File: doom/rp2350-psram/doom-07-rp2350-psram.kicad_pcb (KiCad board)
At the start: 4 copper layers, 144 x 110 mm, 100 parts, among them J4 DM3AT-SF-PEJM5, J5 S2B-PH-K-S(LF)(SN), Q1 AO3401A, Q2 FS8205A, SW1 PTS645SM43SMTR92 LFS, SW10 PTS645SM43SMTR92 LFS, SW11 PTS645SM43SMTR92 LFS, SW12 MSK12C02, SW2 PTS645SM43SMTR92 LFS, SW3 PTS645SM43SMTR92 LFS, SW4 PTS645SM43SMTR92 LFS, SW5 PTS645SM43SMTR92 LFS, SW6 PTS645SM43SMTR92 LFS, SW7 PTS645SM43SMTR92 LFS, SW8 PTS645SM43SMTR92 LFS, SW9 PTS645SM43SMTR92 LFS, U1 RP2350A, U2 W25Q128JVSIQ, U3 APS6404L-3SQR-SN, U4 TLV75533PDBVR, U5 MAX98357AETE+T, U6 BQ24075RGTR, U7 MAX17048G+T10, U8 DW01A, U9 ESD 2-line, Y1 12MHz 10pF

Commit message: doom, examples: re-route around the USB-C receptacle's new land pattern
The standard receptacle became GCT USB4105's recommended layout (pcbkit 7e43c086): its shield
legs moved and two unplated guide holes appeared, under the copper these boards had been routed
with (solder-mask-bridge and clearance errors at J1). `build.run` re-routed the 3–5 nets that
crossed it: all seven check complete with 0 errors again; the six Doom boards export for the fab
without --force.

Claude-Session: https://claude.ai/code/session_01GffCzZXi9ShujPbky1eccg
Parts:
- F1: value PTC 1000mA -> PTC 750mA
- J1: value (none) -> USB4105-GF-A
- U9: value ESD 2-line -> USBLC6-2SC6
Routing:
- net DN: track 52.0 -> 50.7 mm
- net DP: track 64.5 -> 65.3 mm
- net SYS: track 211.8 -> 211.2 mm
- net GND: track 17.2 -> 17.7 mm, vias 20 -> 21

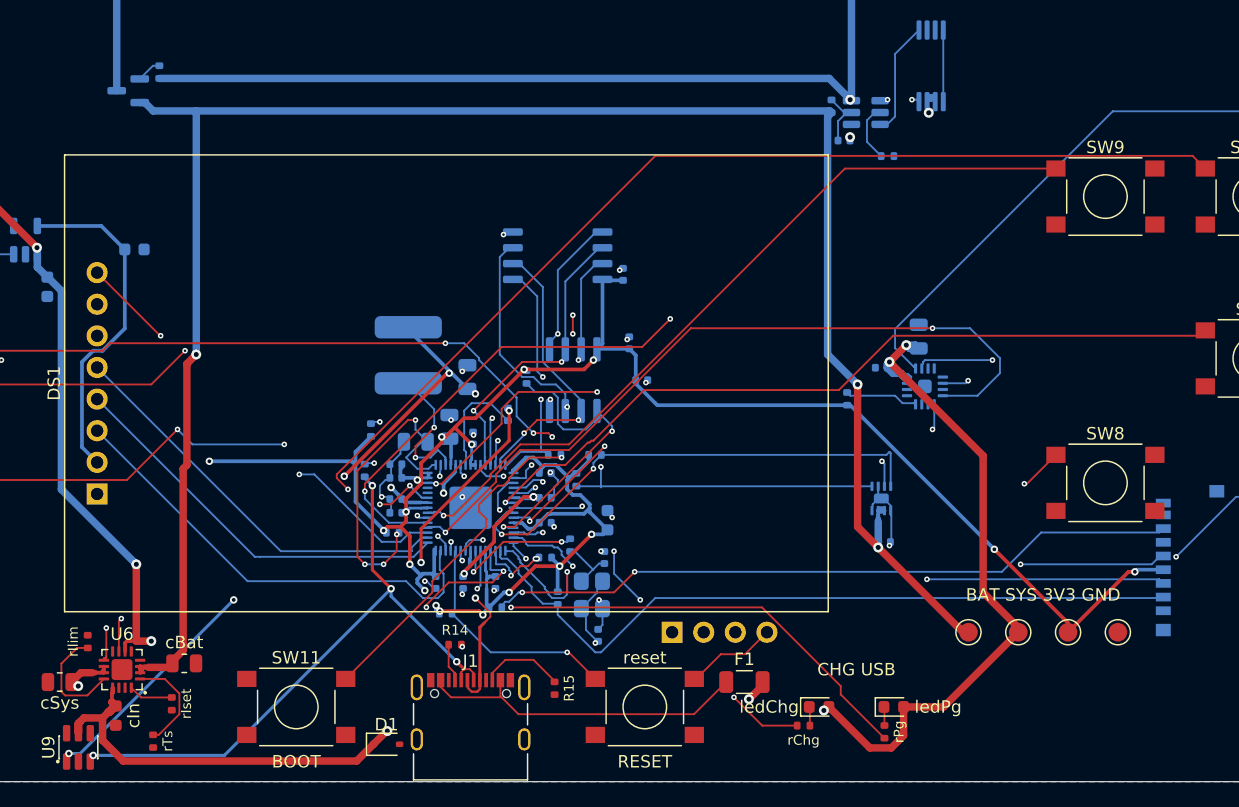
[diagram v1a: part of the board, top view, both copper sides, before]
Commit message: Boards pass check and KiCad 10's DRC again: holes in courtyards, the USB net rename
pcbkit's check now has KiCad 10's pth/npth_inside_courtyard (pcbkit be5b6955), and 13 boards
failed it. KiCad's own DRC (kicad-cli 10) reports the same holes on every one of them.

- Parts that really stand above the holes under them (a screen or a Nano on its sockets, the
  Delta-S02's КМ-6 capacitors flat under its chips, as the factory placed them): a courtyard rule
  for the pair, written to each board's .kicad_dru, so KiCad's DRC agrees.
- Real collisions moved: servo-controller's dial 3 mm up (the Nano's socket pins came out under
  it), c3-pocket's fourth M3 hole from under a cell holder to the top edge's middle, s3-rgb's
  D-pad 2 mm up (a holder's peg came through under the down key).
- v003-emu, c3-pocket, rp2040-tft, rp2350-psram, s3-rgb, teensy41: re-routed for the standard USB
  block's renamed net (usb/raw is usb/vbusIn since pcbkit 2088839e): their tracks still carried
  the old name and shorted the fuse and connector pads.
- p4-touch-7: its board file still had a courtyard for the panel the design gives none (KiCad
  reported 114 courtyard errors); written again.

Measured on the dev host: all 44 registry boards `pcbkit check` complete with 0 errors, and
kicad-cli pcb drc 0 errors on every board.

Claude-Session: https://claude.ai/code/session_018URVYF1YPgyrMNetY9yT1T
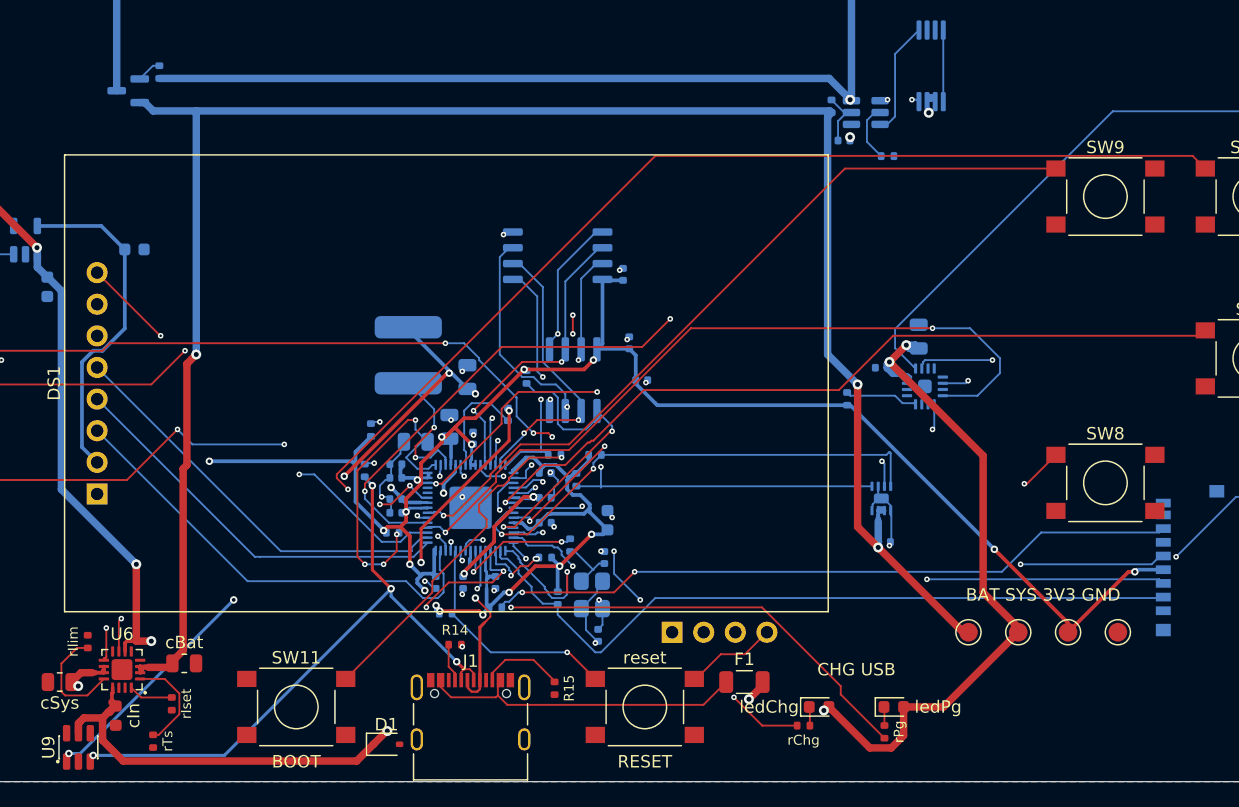
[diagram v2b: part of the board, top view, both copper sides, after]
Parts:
- H1, H2, H3, H4: value (none) -> MountingHole_3.2mm_M3
- J3: value (none) -> PinHeader_1x04_P2.54mm_Vertical
- logo: value (none) -> Logo_PCBKit_pcbkit.io
- tpBat, tpGnd, tpSys, tpV3: value (none) -> TestPoint_Round_D1.5mm
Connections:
- net usb/power/raw renamed usb/power/vbusIn
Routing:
- net VBUS: track 72.9 -> 65.5 mm
- net Net-(C18-1): track 7.14 -> 4.94 mm
- net QSPI_SD3: track 24.2 -> 22.4 mm
- net QSPI_SD0: track 26.2 -> 25.1 mm
- net QSPI_SS: track 20.2 -> 19.2 mm
- net SD_MOSI: track 54.7 -> 53.7 mm
- net SDA: track 40.7 -> 39.9 mm
- net USE: track 46.4 -> 45.6 mm
- net QSPI_SCLK: track 24.9 -> 24.1 mm
- net Net-(R7-1): track 11.3 -> 10.6 mm
- net SYS: track 211.2 -> 210.5 mm
- net usb/power/cc1: track 4.27 -> 3.67 mm
- net usb/power/vbusIn: track 26.9 -> 26.3 mm

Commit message: doom: a resettable fuse per 18650 cell, a 2 % backlight clamp, a 1 A LDO on the S3 boards
The verifier (wiring-parallel-cells) found the two holders of every Doom board directly in parallel:
a cell put in backwards, or one much fuller than the other, drives the other through nothing but
the cells' resistance (about 56-168 A). Each holder's + now reaches BAT_IN through its own 2 A
resettable fuse (Littelfuse 1812L200/16GR, C18198340: 16 V, 100 A interrupting) on new nets
CELL1_P / CELL2_P. Nothing else moved; the boards were re-routed for the new nets.

- s3-rgb: the MT3608 backlight's open-panel clamp was a 28 V 5 % zener (bound 30.0 V against the
  switch's 30 V). It is now two 2 % zeners in series, UDZVTE-1718B + UDZVTE-1710B (27.33-28.56 V;
  LCSC stocks no single 28 V 2 % part). That is under 29.2 V and above the panel's 27.2 V.
- s3-rgb, s3-handheld: TLV75533 (500 mA) -> TLV75733 (1 A, C485517, same DBV pins; sheet from
  SBVS322C), for the ESP32-S3's 500 mA supply peaks (erc-supply-peak).
- c3-pocket, v003-emu: the USB PTC's hold is 750 mA, as the part (nSMD075) is (rating-current).
- pico2-carrier: the CHG/PG LEDs 1.5 mm further from the display's courtyard. rp2350-handheld:
  the logo off the LCD's courtyard and BT1's peg.
- READMEs: the per-cell fuses, the boards already ordered (s3-rgb, JLC W2026102705013253: insert
  the cells one at a time), status and BOM as check and the fab export give them now.

Measured on the dev host (pcbkit 5e0d2cc8): all 11 complete, 0 errors, 0 unrouted. What is left is
erc-rail-name (sent to the verifier as false positives) and full-speed USB pair coupling. The MCU
pins' nets are unchanged on every board, so the firmware and its simulation are unchanged.

Claude-Session: https://claude.ai/code/session_01B3VRfBCg9vAvGVWujVGarr
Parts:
- added F2: PTC 2000mA, Fuse_1812_4532Metric, B.Cu at (126.8, 129.8)
- added F3: PTC 2000mA, Fuse_1812_4532Metric, B.Cu at (126.8, 107.8)
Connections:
- BT1 pad 2: BAT_IN -> CELL1_P
- BT2 pad 2: BAT_IN -> CELL2_P
- SW1 pad 2: UP -> GND
- SW10 pad 2: ENTER -> GND
- SW11 pad 2: BOOTSEL -> GND
- SW2 pad 2: DOWN -> GND
- SW3 pad 2: LEFT -> GND
- SW4 pad 2: RIGHT -> GND
- SW5 pad 2: STRAFE_L -> GND
- SW6 pad 2: STRAFE_R -> GND
- SW7 pad 2: FIRE -> GND
- SW8 pad 2: USE -> GND
- SW9 pad 2: MENU -> GND
- reset pad 2: RUN -> GND
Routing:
- net CELL2_P: track 0.00 -> 6.98 mm
- net CELL1_P: track 0.00 -> 6.98 mm
- net BAT_IN: track 46.0 -> 46.6 mm
